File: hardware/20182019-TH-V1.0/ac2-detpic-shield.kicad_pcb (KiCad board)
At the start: 2 copper layers, 99.1 x 61.6 mm, 52 parts, among them J1 HEADER, J2 HEADER, J3 HEADER, J4 HEADER, J5 HEADER, J6 HEADER, J7 HEADER, M1 M1, M2 M2, M3 MountingHole_2.2mm_M2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

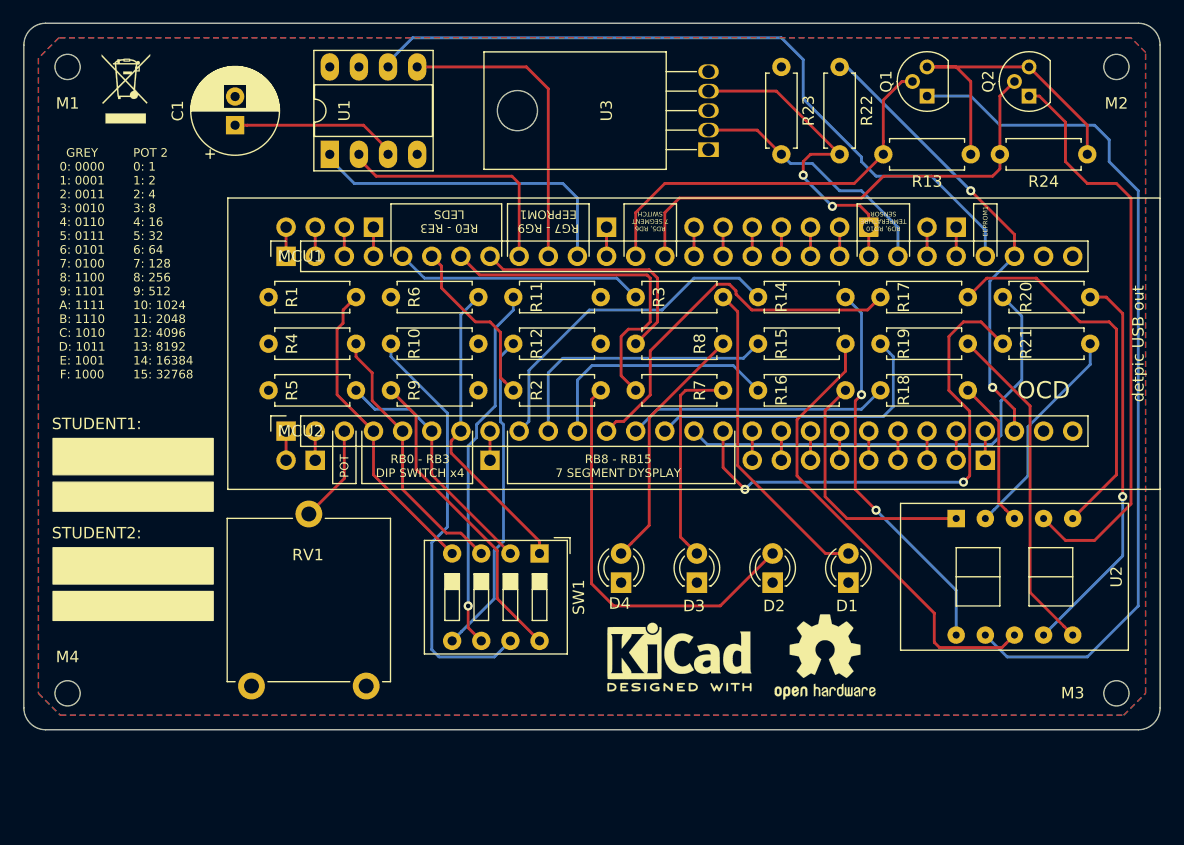
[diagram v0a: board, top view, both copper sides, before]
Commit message: detpic32 size fixed, freeroute files and organization file directory changes
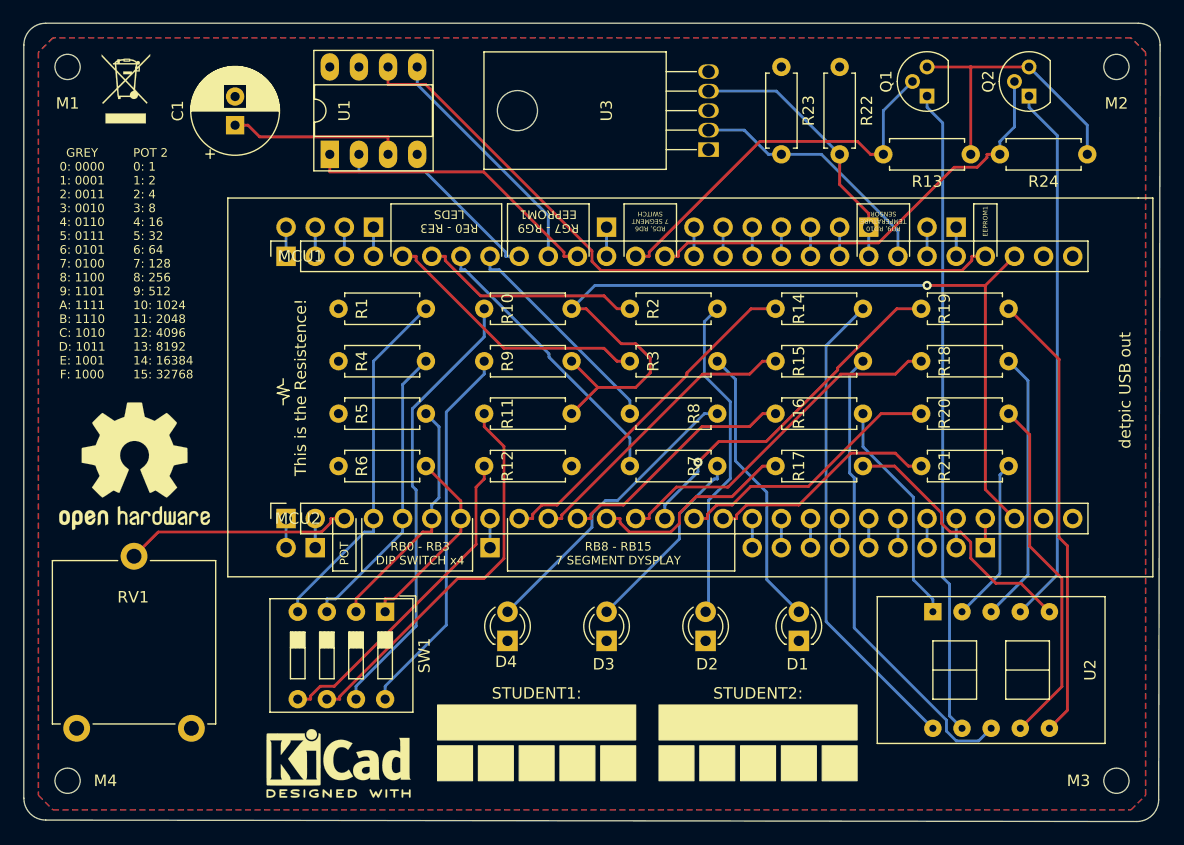
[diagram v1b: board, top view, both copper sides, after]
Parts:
- removed REF**: OSHW-Logo2_9.8x8mm_SilkScreen, Symbol:OSHW-Logo2_9.8x8mm_SilkScreen
- added REF2: OSHW-Logo2_14.6x12mm_SilkScreen, Symbol:OSHW-Logo2_14.6x12mm_SilkScreen, F.Cu at (136.7, 64.0)
- added REF3: KiCad-Logo2_5mm_SilkScreen, Symbol:KiCad-Logo2_5mm_SilkScreen, F.Cu at (154.4, 89.9)
- REF4: renamed from REF**; moved to B.Cu
- moved REF4 42.7 mm to (220.0, 57.4), turned to 270 degrees
- moved R17 17.3 mm to (200.2, 64.0)
- moved RV1 15.7 mm to (141.6, 86.9)
- moved R6 15.4 mm to (162.1, 64.0)
- moved SW1 14.4 mm to (158.5, 76.7)
- moved R21 12.8 mm to (212.9, 64.0)
- moved R2 12.4 mm to (187.5, 50.3)
- moved R20 12.4 mm to (212.9, 59.4)
- moved D4 11.1 mm to (169.2, 79.2)
- moved R12 11.0 mm to (174.8, 64.0)
- moved R11 10.5 mm to (174.8, 59.4)
- moved D3 9.37 mm to (177.8, 79.2)
- moved R10 8.68 mm to (174.8, 50.3)
- moved R9 8.52 mm to (174.8, 54.9)
- moved U2 8.38 mm to (211.3, 81.8)
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- renumbered REF** to REF1
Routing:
- net /+3.3V: track 40.2 -> 83.4 mm, vias 2 -> 1
- net /RB15: track 44.9 -> 20.3 mm, vias 2 -> 0
- net Net-(Q1-Pad1): track 75.1 -> 56.4 mm
- net /RB14: track 41.1 -> 23.8 mm
- net /RB11: track 33.0 -> 18.3 mm
- net /RB4: track 8.51 -> 19.9 mm
- net Net-(R18-Pad1): track 12.9 -> 23.9 mm
- net Net-(R17-Pad1): track 33.6 -> 22.9 mm
- net Net-(R19-Pad1): track 29.2 -> 39.3 mm
- net /RB0: track 26.5 -> 17.2 mm
- net /RB12: track 22.8 -> 30.8 mm
- net Net-(R14-Pad1): track 33.9 -> 41.8 mm, vias 2 -> 0
- net Net-(D2-Pad2): track 35.7 -> 28.7 mm
- net Net-(R9-Pad2): track 27.2 -> 33.0 mm
- net /RD10: track 29.3 -> 23.7 mm, vias 2 -> 0
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- added copper zone on B.Cu, net /+3.3V
- added copper zone on F.Cu, net GND
- removed copper zone on F.Cu, net /+3.3V
- removed copper zone on B.Cu, net GND
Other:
- board size 99.1 x 61.6 mm -> 99.1 x 69.6 mm
- board text added: "This is the Resistence!"
- board text removed: "OCD"

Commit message: added gnd test point to 20182019-TH v1.1
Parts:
- added grab your GND here: Test Point GND, TestPoint:TestPoint_Pad_2.5x2.5mm, F.Cu at (138.3, 92.6)
- SW1: value DIP SWITCH x4 -> SW_DIP_x04
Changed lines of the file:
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@@
   (general
     (thickness 1.6)
-    (drawings 75)
+    (drawings 83)
     (tracks 327)
     (zones 0)
-    (modules 53)
+    (modules 54)
     (nets 75)
   )
@@
     (add_net "Net-(R9-Pad2)")
   )
+  (module TestPoint:TestPoint_Pad_2.5x2.5mm (layer F.Cu)
+    (at 138.303 92.583)
+    (descr "SMD rectangular pad as test Point, square 2.5mm side length")
+    (tags "test point SMD pad rectangle square")
+    (attr virtual)
+    (fp_text reference "grab your GND here" (at 1.524 -3.302) (layer F.SilkS)
+      (effects (font (size 0.5 0.5) (thickness 0.125)))
+    )
+    (fp_text value "Test Point GND" (at 0.381 5.08) (layer F.Fab)
+      (effects (font (size 1 1) (thickness 0.15)))
+    )
+    (fp_text user %R (at -6.858 5.08) (layer F.Fab)
+      (effects (font (size 1 1) (thickness 0.15)))
+    )
+    (pad 1 smd rect (at 0 0) (size 3.81 2.5) (layers F.Cu F.Mask)
+      (net 2 GND))
+    (pad 1 thru_hole roundrect (at 0 -1.27) (size 3.81 1.524) (drill oval 3.2 0.762) (layers *.Cu *.Mask) (roundrect_rratio 0.35)
+      (net 2 GND))
+  )
   (module Symbol:KiCad-Logo2_5mm_SilkScreen (layer F.Cu)
     (at 154.432 89.916)
@@
     (tags "Logo KiCad")
     (attr virtual)
-    (fp_text reference REF3 (at -0.508 7.112) (layer F.SilkS) hide
+    (fp_text reference REF3 (at -0.889 7.62) (layer F.SilkS) hide
       (effects (font (size 1 1) (thickness 0.15)))
     )
-    (fp_text value KiCad-Logo2_5mm_SilkScreen (at 0 5.08) (layer F.Fab) hide
+    (fp_text value KiCad-Logo2_5mm_SilkScreen (at -1.397 6.096) (layer F.Fab) hide
       (effects (font (size 1 1) (thickness 0.15)))
     )
@@
     (tags "mounting hole 2.2mm no annular m2")
     (attr virtual)
-    (fp_text reference M4 (at 3.302 0) (layer F.SilkS)
+    (fp_text reference M4 (at -2.54 -2.413) (layer F.SilkS)
       (effects (font (size 1 1) (thickness 0.15)))
     )
@@
       (effects (font (size 1 1) (thickness 0.15)))
     )
-    (fp_text value "DIP SWITCH x4" (at 3.937 11.303 270) (layer F.Fab)
+    (fp_text value SW_DIP_x04 (at 3.937 11.303 270) (layer F.Fab)
       (effects (font (size 1 1) (thickness 0.15)))
     )
@@
     )
   )
+  (gr_line (start 144.145 89.408) (end 143.891 89.408) (layer F.SilkS) (width 0.12))
+  (gr_line (start 144.145 89.662) (end 144.145 89.408) (layer F.SilkS) (width 0.12))
+  (gr_line (start 141.605 91.186) (end 144.145 91.186) (layer F.SilkS) (width 0.12))
+  (gr_line (start 141.605 91.313) (end 141.351 91.186) (layer F.SilkS) (width 0.12))
+  (gr_line (start 141.605 91.059) (end 141.605 91.313) (layer F.SilkS) (width 0.12))
+  (gr_line (start 141.351 91.186) (end 141.605 91.059) (layer F.SilkS) (width 0.12))
+  (gr_line (start 144.145 91.059) (end 144.145 91.186) (layer F.SilkS) (width 0.12))
+  (gr_line (start 144.145 89.662) (end 144.145 91.059) (layer F.SilkS) (width 0.12))
   (gr_line (start 149.606 56.896) (end 149.606 56.388) (layer F.SilkS) (width 0.12))
   (gr_line (start 149.098 57.15) (end 149.606 56.896) (layer F.SilkS) (width 0.12))
